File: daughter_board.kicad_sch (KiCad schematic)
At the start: 9 parts, among them J2 Conn_02x25_Odd_Even, SW1 SW_Push

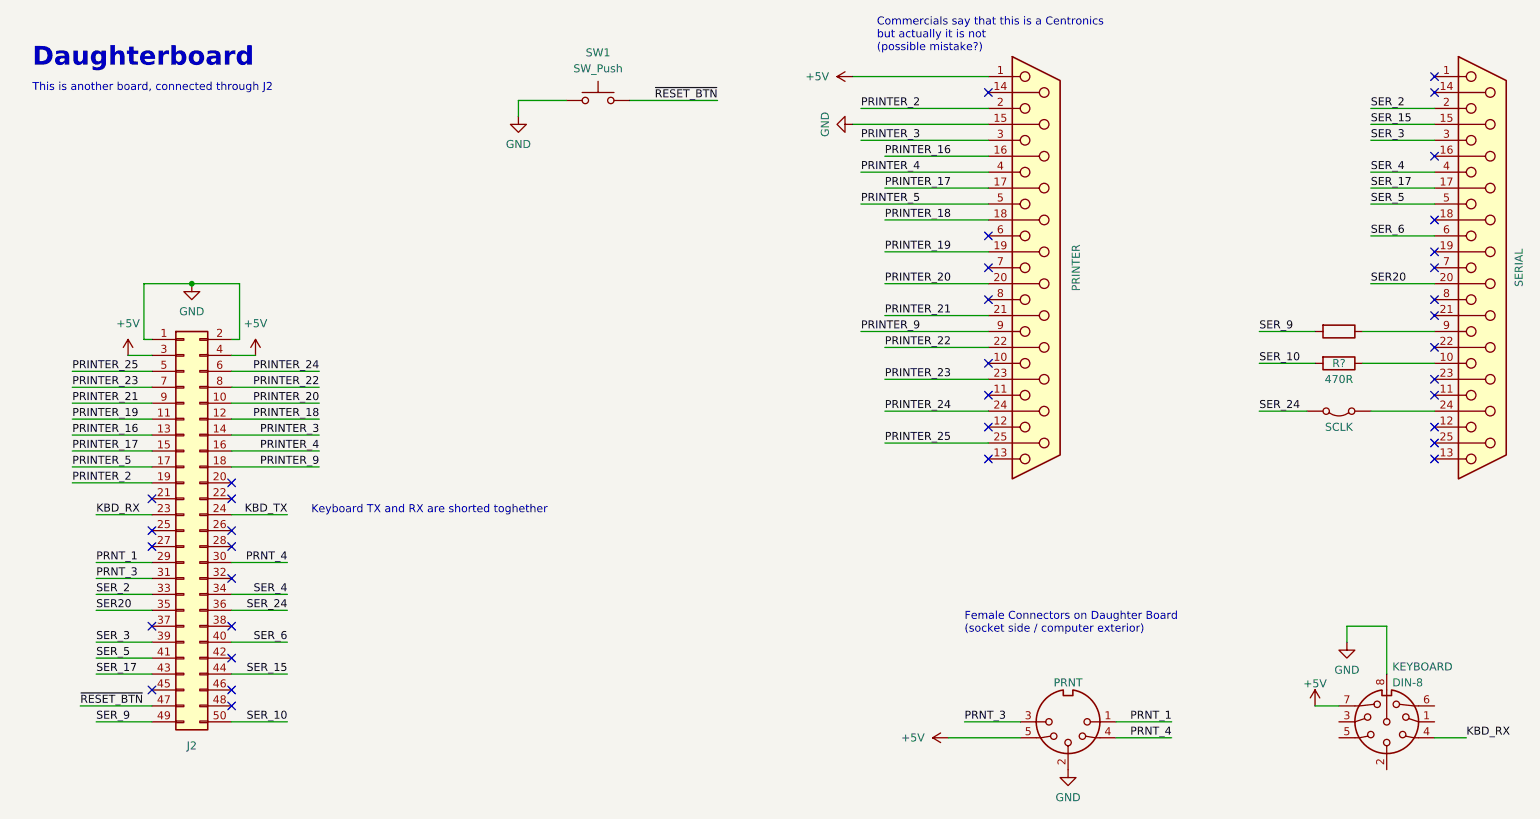
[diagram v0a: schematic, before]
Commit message: drc: fixed labels
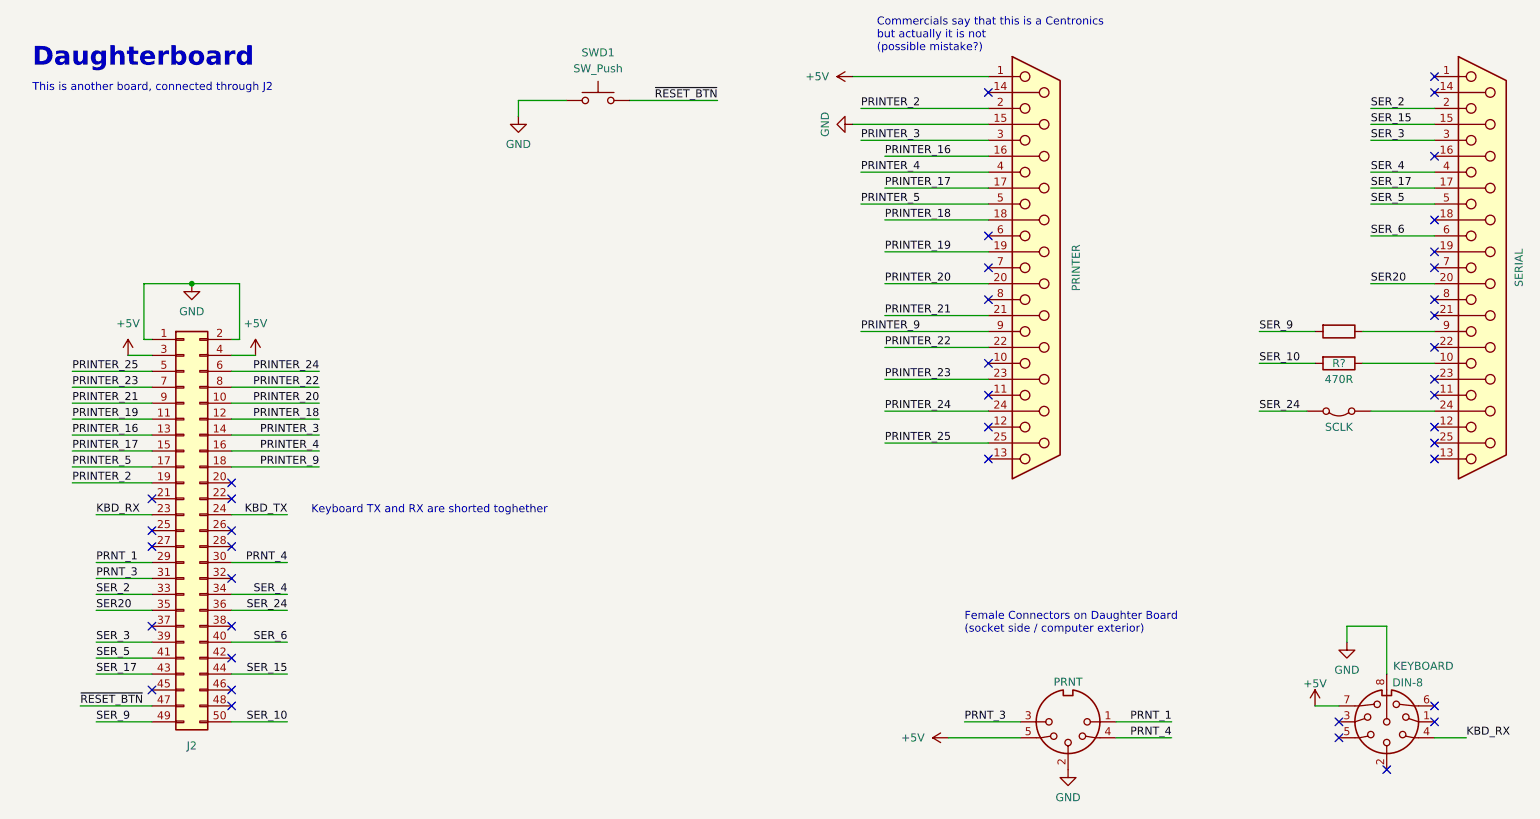
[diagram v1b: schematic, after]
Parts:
- renumbered SW1 to SWD1
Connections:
- no-connect marks 36 -> 41
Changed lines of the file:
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@@
+	)
+	(no_connect
+		(at 248.92 127)
+	)
+	(no_connect
+		(at 233.68 129.54)
 	)
 	(no_connect
@@
 	)
 	(no_connect
+		(at 233.68 132.08)
+	)
+	(no_connect
 		(at 57.15 127)
 	)
@@
 	)
 	(no_connect
+		(at 248.92 129.54)
+	)
+	(no_connect
 		(at 248.92 26.67)
+	)
+	(no_connect
+		(at 241.3 137.16)
 	)
 	(no_connect
@@
 		(on_board yes)
 		(dnp no)
-		(fields_autoplaced yes)
 		(property "Reference" "KEYBOARD"
 			(at 242.1889 120.7602 0)
@@
 				)
 				(justify right)
+				(hide yes)
 			)
 		)
@@
 			)
 		)
-		(property "Description" ""
-			(at 241.3 129.54 0)
+		(property "Description" "KEYBOARD"
+			(at 247.142 120.65 0)
 			(effects
 				(font
@@
 		(on_board yes)
 		(dnp no)
-		(fields_autoplaced yes)
 		(property "Reference" "PRINTER"
 			(at 191.77 57.15 90)
@@
 					(size 1.27 1.27)
 				)
+				(hide yes)
 			)
 		)
@@
 			)
 		)
-		(property "Datasheet" " ~"
+		(property "Datasheet" "~"
 			(at 185.42 57.15 0)
 			(effects
@@
 			)
 		)
-		(property "Description" ""
-			(at 185.42 57.15 0)
+		(property "Description" "PRINTER"
+			(at 191.77 57.15 90)
 			(effects
 				(font
@@
 		(dnp no)
 		(fields_autoplaced yes)
-		(property "Reference" "SW1"
+		(property "Reference" "SWD1"
 			(at 115.57 22.86 0)
 			(effects
@@
 			(project "ceda"
 				(path "/12a6dbe3-008d-4c5b-88f6-9f1c816060be/4f1cc97c-1ae7-488a-96b4-ad54fee0fde4"
-					(reference "SW1")
+					(reference "SWD1")
 					(unit 1)
 				)
@@
 		(on_board yes)
 		(dnp no)
-		(fields_autoplaced yes)
 		(property "Reference" "SERIAL"
 			(at 262.3804 57.15 90)
@@
 					(size 1.27 1.27)
 				)
+				(hide yes)
 			)
 		)
@@
 			)
 		)
-		(property "Datasheet" " ~"
+		(property "Datasheet" "~"
 			(at 256.54 57.15 0)
 			(effects
@@
 			)
 		)
-		(property "Description" ""
-			(at 256.54 57.15 0)
+		(property "Description" "SERIAL"
+			(at 262.382 57.15 90)
 			(effects
 				(font
@@
 		(on_board yes)
 		(dnp no)
-		(fields_autoplaced yes)
 		(property "Reference" "PRNT"
 			(at 190.4999 123.2972 0)
@@
 					(size 1.27 1.27)
 				)
+				(hide yes)
 			)
 		)
@@
 			)
 		)
-		(property "Description" ""
-			(at 190.5 129.54 0)
-			(effects
-				(font
+		(property "Description" "PRNT"
+			(at 190.5 123.19 0)
+			(effects
+				(font

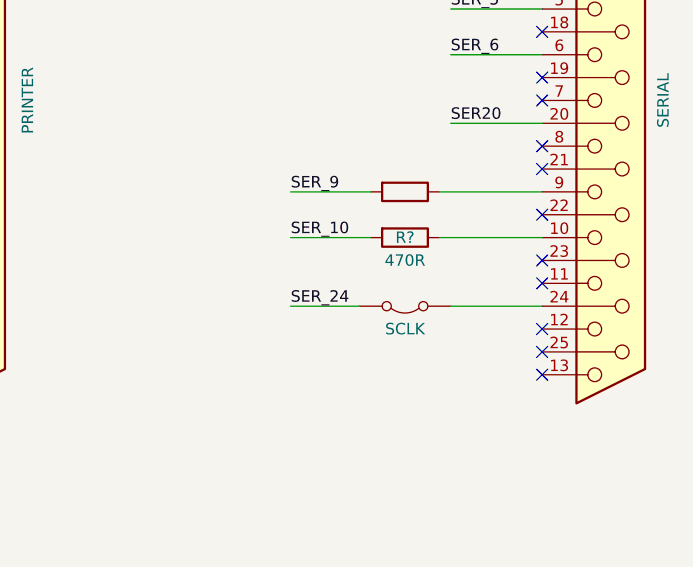
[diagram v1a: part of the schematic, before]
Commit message: Annotated all components
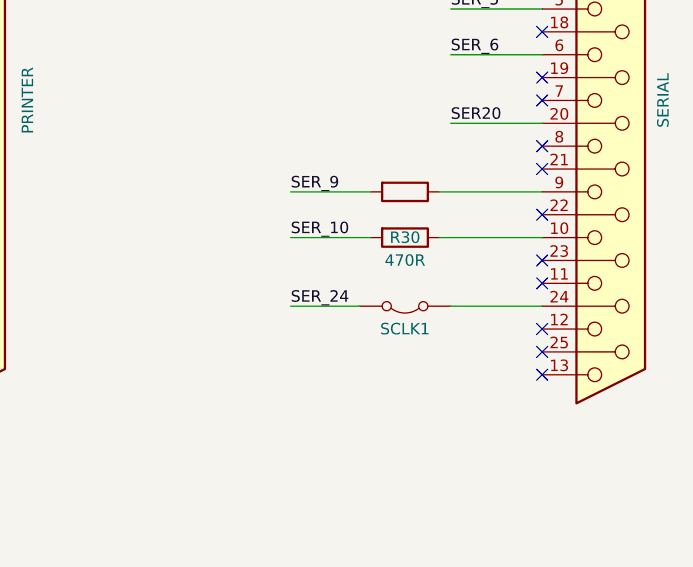
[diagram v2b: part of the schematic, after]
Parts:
- gave numbers to parts that had none: 2
- renumbered KEYBOARD to KEYBOARD1, PRINTER to PRINTER1, PRNT to PRNT1, SCLK to SCLK1, SERIAL to SERIAL1
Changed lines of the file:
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@@
 		(on_board yes)
 		(dnp no)
-		(property "Reference" "KEYBOARD"
+		(property "Reference" "KEYBOARD1"
 			(at 242.1889 120.7602 0)
 			(effects
@@
 			(project "ceda"
 				(path "/12a6dbe3-008d-4c5b-88f6-9f1c816060be/4f1cc97c-1ae7-488a-96b4-ad54fee0fde4"
-					(reference "KEYBOARD")
+					(reference "KEYBOARD1")
 					(unit 1)
 				)
@@
 		(on_board yes)
 		(dnp no)
-		(property "Reference" "PRINTER"
+		(property "Reference" "PRINTER1"
 			(at 191.77 57.15 90)
 			(effects
@@
 			(project "ceda"
 				(path "/12a6dbe3-008d-4c5b-88f6-9f1c816060be/4f1cc97c-1ae7-488a-96b4-ad54fee0fde4"
-					(reference "PRINTER")
+					(reference "PRINTER1")
 					(unit 1)
 				)
@@
 		(dnp no)
 		(fields_autoplaced yes)
-		(property "Reference" "SCLK"
+		(property "Reference" "SCLK1"
 			(at 233.68 82.55 0)
 			(effects
@@
 			(project "ceda"
 				(path "/12a6dbe3-008d-4c5b-88f6-9f1c816060be/4f1cc97c-1ae7-488a-96b4-ad54fee0fde4"
-					(reference "SCLK")
+					(reference "SCLK1")
 					(unit 1)
 				)
@@
 		(on_board yes)
 		(dnp no)
-		(property "Reference" "SERIAL"
+		(property "Reference" "SERIAL1"
 			(at 262.3804 57.15 90)
 			(effects
@@
 			(project "ceda"
 				(path "/12a6dbe3-008d-4c5b-88f6-9f1c816060be/4f1cc97c-1ae7-488a-96b4-ad54fee0fde4"
-					(reference "SERIAL")
+					(reference "SERIAL1")
 					(unit 1)
 				)
@@
 		(on_board yes)
 		(dnp no)
-		(property "Reference" "R?"
+		(property "Reference" "R30"
 			(at 233.68 72.39 90)
 			(effects
@@
 			(project "ceda"
 				(path "/12a6dbe3-008d-4c5b-88f6-9f1c816060be/4f1cc97c-1ae7-488a-96b4-ad54fee0fde4"
-					(reference "R?")
+					(reference "R30")
 					(unit 1)
 				)
@@
 		(dnp no)
 		(fields_autoplaced yes)
-		(property "Reference" "R?"
+		(property "Reference" "R23"
 			(at 233.68 60.96 90)
 			(effects
@@
 			(project "ceda"
 				(path "/12a6dbe3-008d-4c5b-88f6-9f1c816060be/4f1cc97c-1ae7-488a-96b4-ad54fee0fde4"
-					(reference "R?")
+					(reference "R23")
 					(unit 1)
 				)
@@
 		(on_board yes)
 		(dnp no)
-		(property "Reference" "PRNT"
+		(property "Reference" "PRNT1"
 			(at 190.4999 123.2972 0)
 			(effects
@@
 			(project "ceda"
 				(path "/12a6dbe3-008d-4c5b-88f6-9f1c816060be/4f1cc97c-1ae7-488a-96b4-ad54fee0fde4"
-					(reference "PRNT")
-					(unit 1)
-				)
+					(reference "PRNT1")
+					(unit 1)
+				)

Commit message: pcb: added and placed almost all components
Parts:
- J2: footprint (none) -> Connector_PinHeader_2.54mm:PinHeader_2x25_P2.54mm_Vertical
- R30: footprint (none) -> Resistor_THT:R_Axial_DIN0204_L3.6mm_D1.6mm_P5.08mm_Vertical
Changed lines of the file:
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@@
 			)
 		)
-		(property "Footprint" ""
+		(property "Footprint" "Connector_PinHeader_2.54mm:PinHeader_2x25_P2.54mm_Vertical"
 			(at 49.53 99.06 0)
 			(effects
@@
 			)
 		)
-		(property "Footprint" ""
+		(property "Footprint" "Resistor_THT:R_Axial_DIN0204_L3.6mm_D1.6mm_P5.08mm_Vertical"
 			(at 233.68 70.612 90)
 			(effects

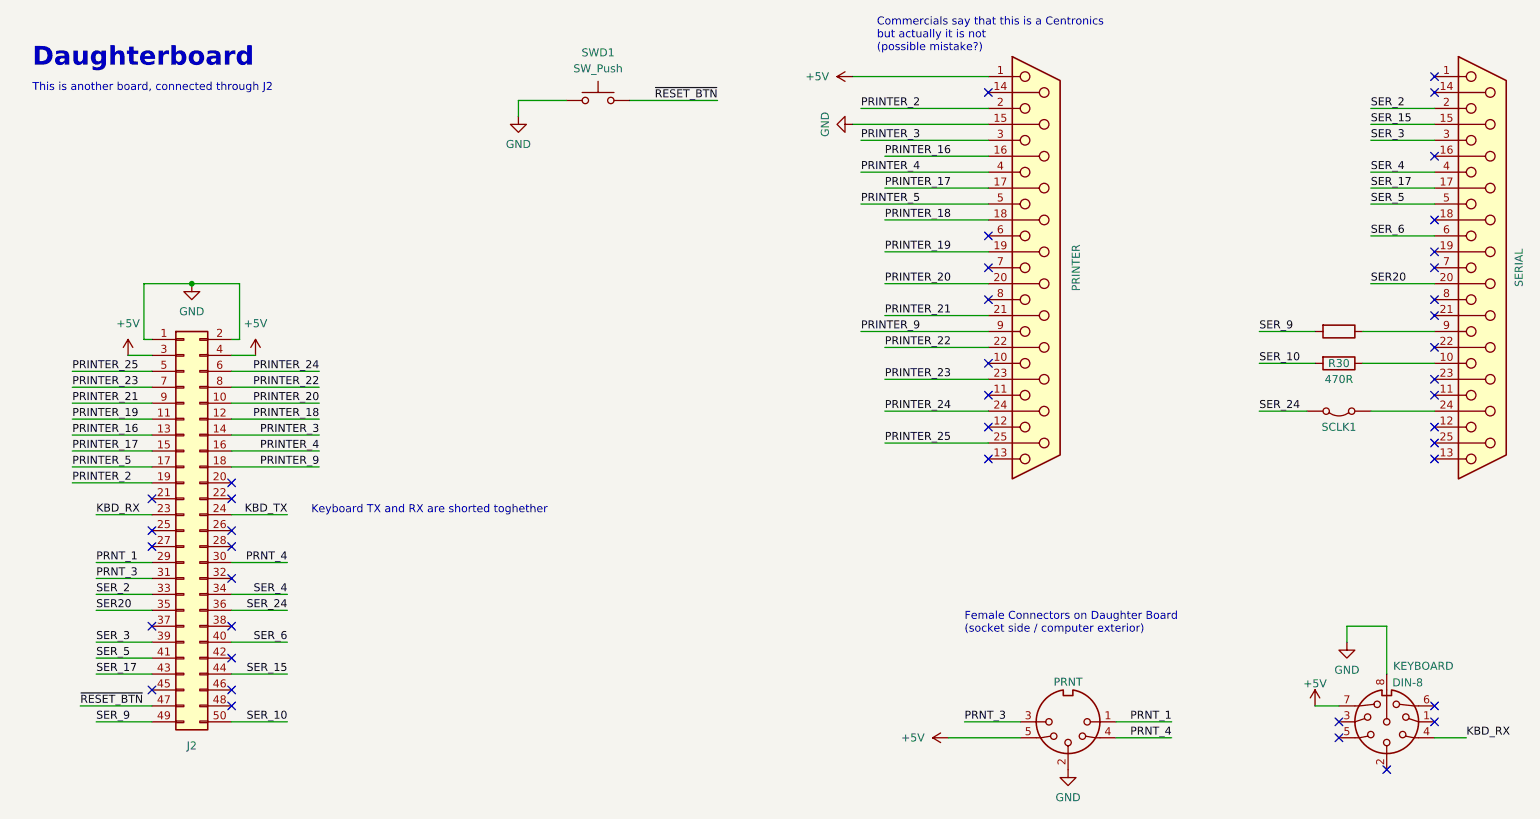
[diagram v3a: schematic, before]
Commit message: pcb: added all the connector, 99% routed
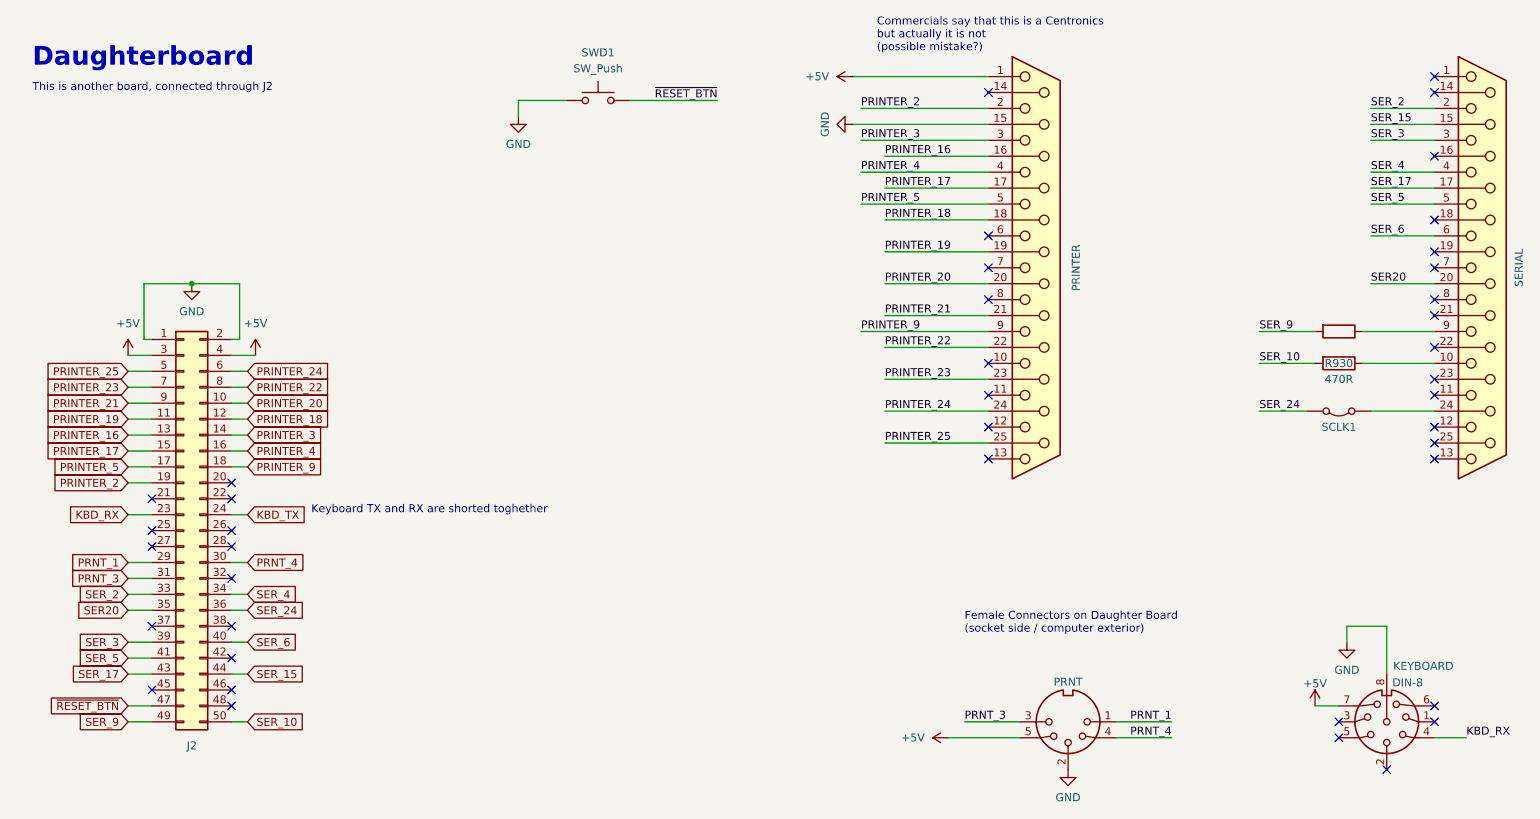
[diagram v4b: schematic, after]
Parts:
- R930: renamed from R30; footprint Resistor_THT:R_Axial_DIN0204_L3.6mm_D1.6mm_P5.08mm_Vertical -> (none)

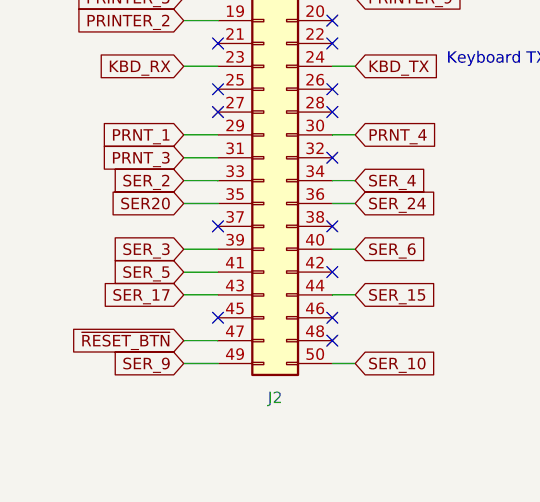
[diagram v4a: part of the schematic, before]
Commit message: sch: +12v in daughterboard connector
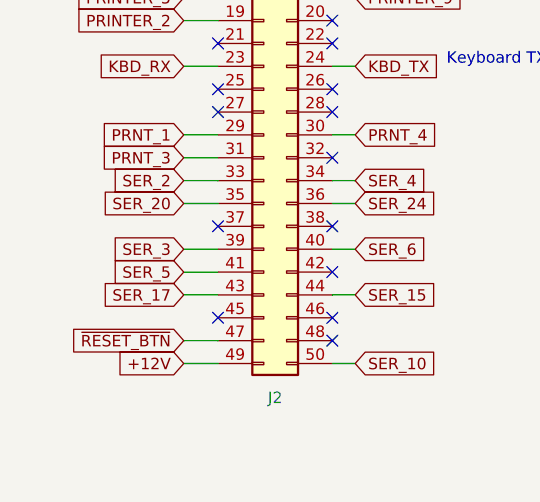
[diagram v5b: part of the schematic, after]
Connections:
- net SER20: no longer J2.35 (Pin_35)
- net SER_9: no longer J2.49 (Pin_49)
- new net +12V: J2.49 (Pin_49)
- new net SER_20: J2.35 (Pin_35)
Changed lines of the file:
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@@
 		)
 	)
-	(global_label "SER_9"
+	(global_label "+12V"
 		(shape input)
 		(at 40.64 129.54 180)
@@
 		)
 		(property "Intersheetrefs" "${INTERSHEET_REFS}"
-			(at 31.8492 129.54 0)
+			(at 32.5748 129.54 0)
 			(effects
 				(font
@@
 		)
 	)
-	(global_label "SER20"
+	(global_label "SER_20"
 		(shape input)
 		(at 40.64 111.76 180)
@@
 		)
 		(property "Intersheetrefs" "${INTERSHEET_REFS}"
-			(at 31.6073 111.76 0)
-			(effects
-				(font
+			(at 30.6397 111.76 0)
+			(effects
+				(font

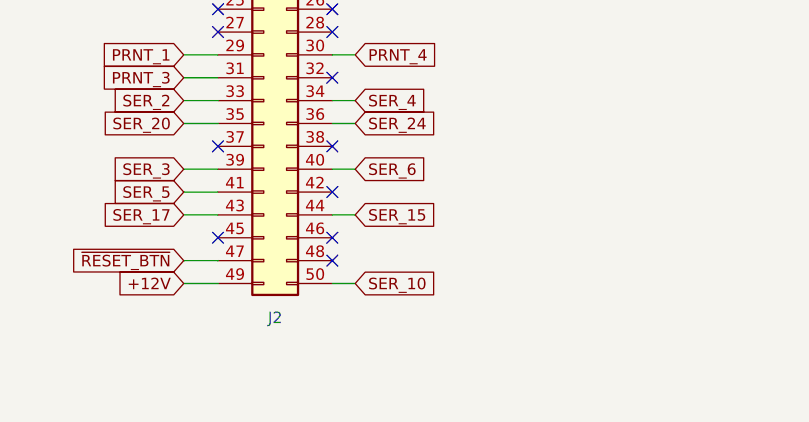
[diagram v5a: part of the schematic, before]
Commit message: pcb: fixed traces
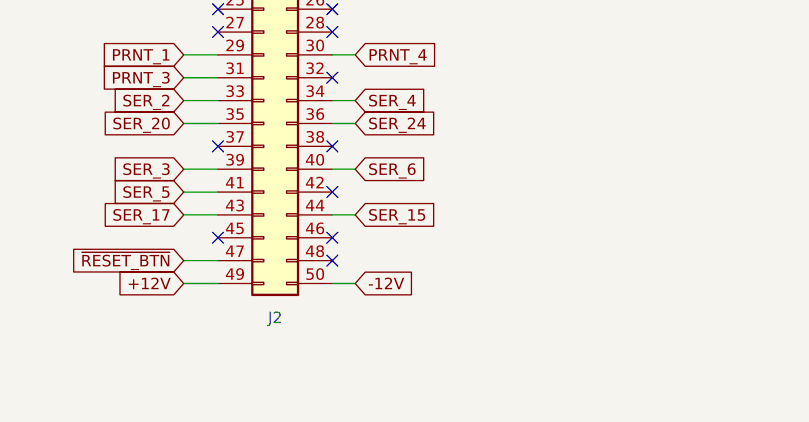
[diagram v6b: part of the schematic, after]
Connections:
- net SER_10: no longer J2.50 (Pin_50)
- new net -12V: J2.50 (Pin_50)
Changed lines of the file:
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@@
 		)
 	)
-	(global_label "SER_10"
+	(global_label "-12V"
 		(shape input)
 		(at 59.69 129.54 0)
@@
 		)
 		(property "Intersheetrefs" "${INTERSHEET_REFS}"
-			(at 69.6903 129.54 0)
+			(at 67.7552 129.54 0)
 			(effects
 				(font
